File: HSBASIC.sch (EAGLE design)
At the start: 25 parts, among them IC1 ESP12SMT, IC3 MS563702BA03, IC4 DHT12

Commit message: Routing
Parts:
- removed R3: 10K, freetronics-jon:RESISTOR0603
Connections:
- removed net N$11: LED3.A, R7.1
- new net N$5: LED2.C, R10.2
- net 3.3V: now also LED2.A, LED3.A; no longer R3.2
- net GND: no longer LED2.C, LED3.C
- net GPIO16: no longer R10.2, R7.2
- net GPIO2: now also R10.1, R7.1; no longer R3.1
- net N$4: now also LED3.C, R7.2; no longer LED2.A, R10.1
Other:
- note added: "Change sensor to BME280. 20 bought in Jan 2018. Find them! Barometric Pressure Sensor: MS5637-02BA03 Pressure range: 1kpa to 200kpa (0.145psi to 29psi) Temperature range: -40C to +85C Temperature resolution: 0.01C Temperature accuracy: +/- 1C I2C address: 0xED Humidity / Temperature Sensor: DHT12 Humidity range: 20 to 95% Humidity resolution: 0.1% Humidity precision: +/- 5% Temperature range: -20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"
- note added: "GPIO0: Bias HIGH GPIO2: Bias HIGH GPIO15: Bias LOW CH_PD: Bias HIGH GPIO2: Status LED active low From D1 Mini profile for Arduino: GPIO4: D2 SDA GPIO5: D1 SCL From Sonoff: GPIO2: SDA GPIO14: SCL From Tasmota: GPIO4: SDA GPIO14: SCL"
- note removed: "Barometric Pressure Sensor: MS5637-02BA03 Pressure range: 1kpa to 200kpa (0.145psi to 29psi) Temperature range: -40C to +85C Temperature resolution: 0.01C Temperature accuracy: +/- 1C I2C address: 0xED Humidity / Temperature Sensor: DHT12 Humidity range: 20 to 95% Humidity resolution: 0.1% Humidity precision: +/- 5% Temperature range: -20 to +60C Temperature resolution: 0.1C Temperature precision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"
- note removed: "GPIO0: Bias HIGH GPIO2: Bias HIGH GPIO15: Bias LOW CH_PD: Bias HIGH GPIO16: Status LED From D1 Mini profile for Arduino: GPIO4: D2 SDA GPIO5: D1 SCL From Sonoff: GPIO2: SDA GPIO14: SCL From Tasmota: GPIO4: SDA GPIO14: SCL"
- moved on the sheet: LED2, LED3, R10, R7

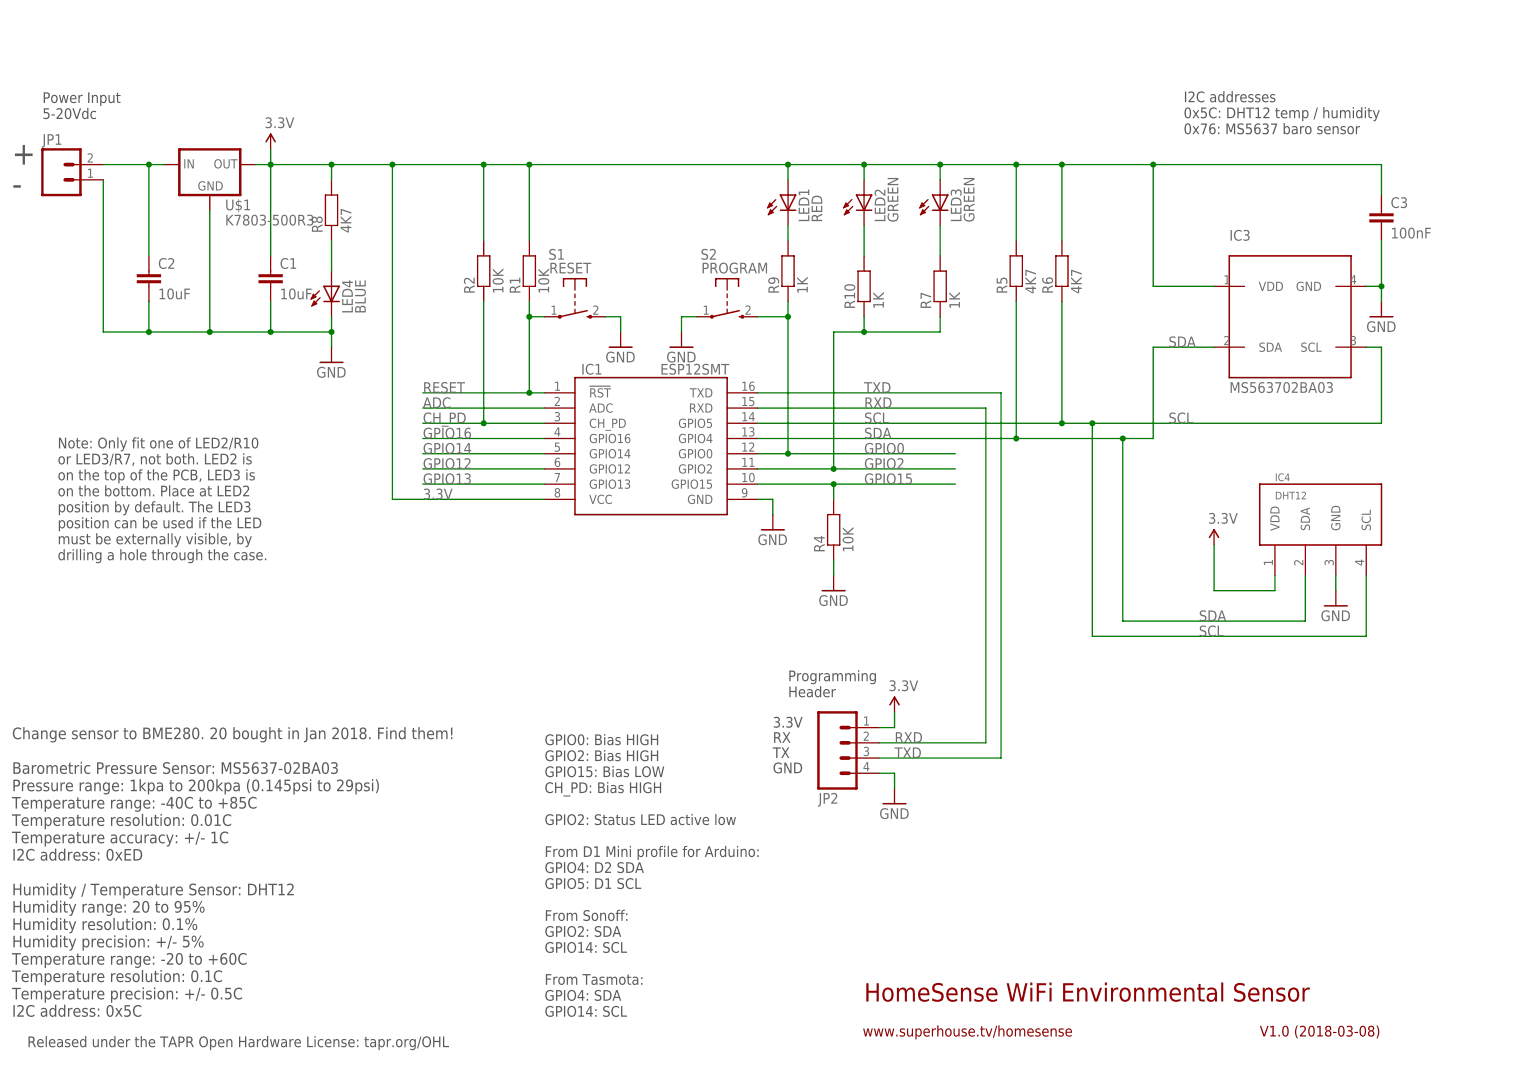
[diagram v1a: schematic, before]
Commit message: Switch to BME280 sensor for Tasmota compatibility
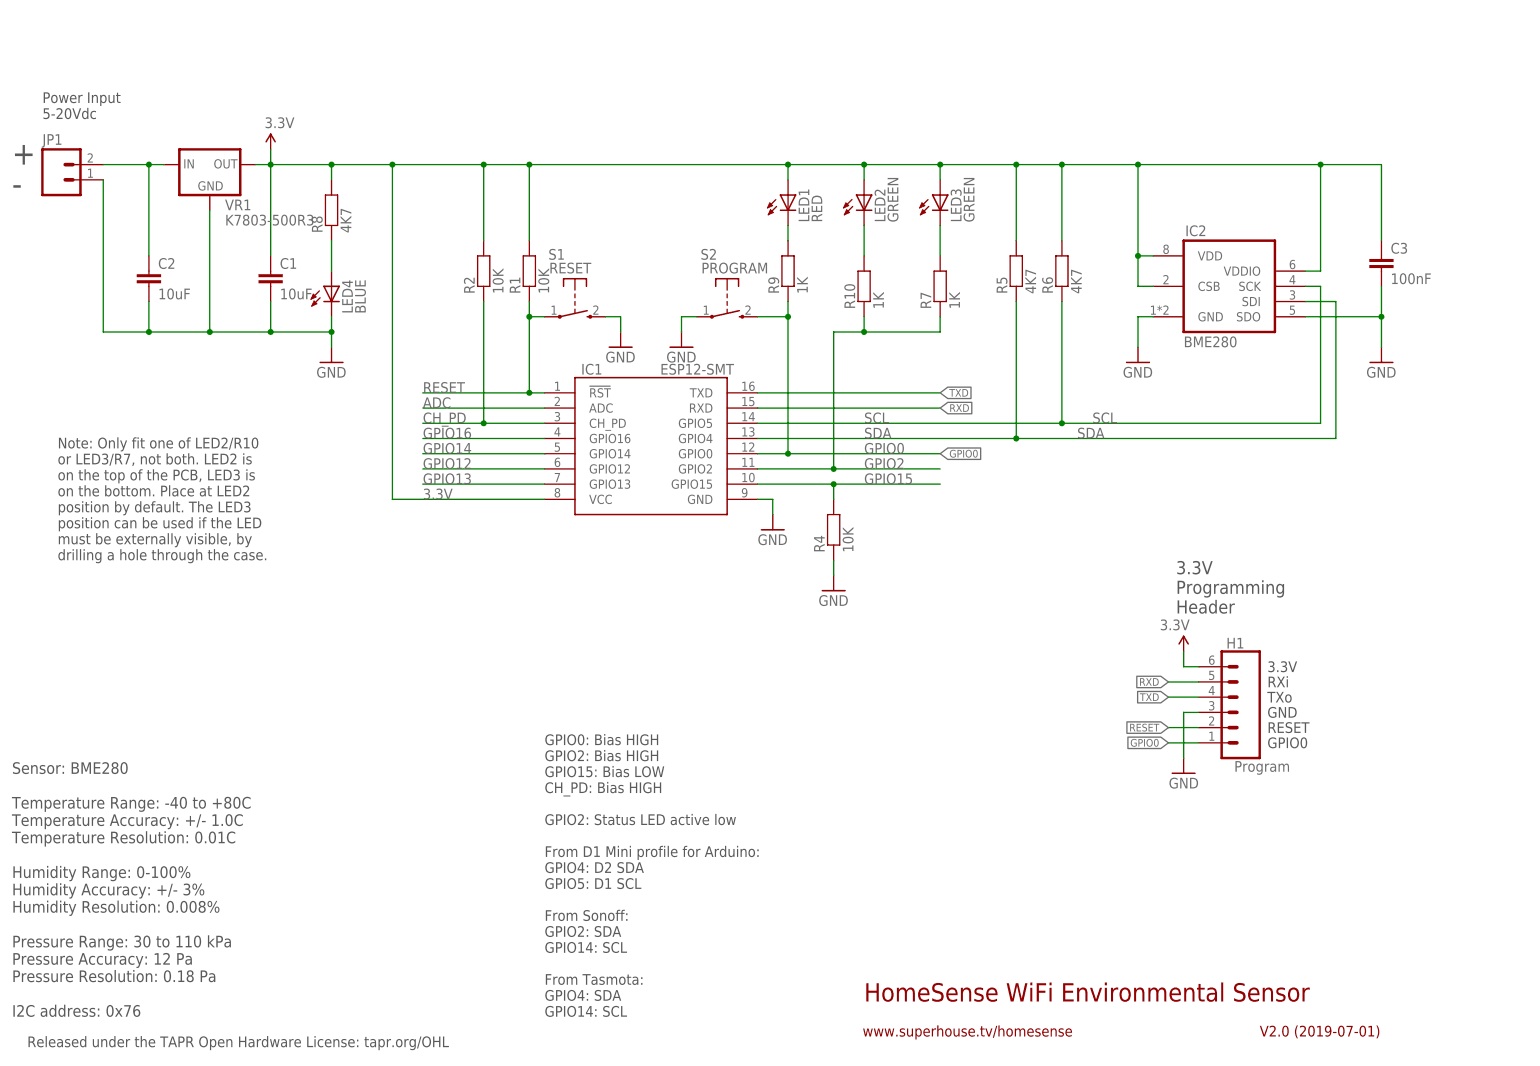
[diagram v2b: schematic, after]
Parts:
- removed IC3: MS563702BA03, freetronics-jon:MS563702BA03
- removed IC4: DHT12, freetronics-jon:DHT12FLAT
- removed JP2: (no value), freetronics-jon:M04PTH
- removed U$1: K7803-500R3, freetronics-jon:K78XX-500R3
- added H1: Program, SuperHouse-Connectors:M06-SOCKET
- added IC2: BME280, SuperHouse-Sensors:BME280
- added VR1: K7803-500R3, SuperHouse-Regulators:K78XX-500R3
- C1, C2: device freetronics-jon:CAP0805 -> SuperHouse-DiscreteSemi:CAP1206
- C3: device freetronics-jon:CAP0603 -> SuperHouse-DiscreteSemi:CAP0603
- IC1: value ESP12SMT -> ESP12-SMT; device freetronics-jon:ESP12SMT -> SuperHouse-MCUs:ESP12-SMT
- LED1, LED2, LED3, LED4: device freetronics-jon:LED0603 -> SuperHouse-LEDs:LED0603
- R1, R10, R2, R4, R5, R6, R7, R8, R9: device freetronics-jon:RESISTOR0603 -> SuperHouse-DiscreteSemi:RESISTOR0603
- S1, S2: device freetronics-jon:TAC_SWITCH_2PINSMT -> SuperHouse-Switches:TAC_SWITCH_2PINSMT
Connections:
- net 3.3V: now also H1.6, IC2.CSB, IC2.VDD, IC2.VDDIO, VR1.OUT; no longer IC3.VDD, IC4.VDD, JP2.1, U$1.OUT
- net GND: now also H1.3, IC2.GND, IC2.SDO, VR1.GND; no longer IC3.GND, IC4.GND, JP2.4, U$1.GND
- net GPIO0: now also H1.1
- net N$1: now also VR1.IN; no longer U$1.IN
- net RESET: now also H1.2
- net RXD: now also H1.5; no longer JP2.2
- net SCL: now also IC2.SCK; no longer IC3.SCL, IC4.SCL
- net SDA: now also IC2.SDI; no longer IC3.SDA, IC4.SDA
- net TXD: now also H1.4; no longer JP2.3
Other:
- note added: "3.3V Programming Header"
- note added: "GPIO0"
- note added: "RESET"
- note added: "RXi"
- note added: "Sensor: BME280 Temperature Range: -40 to +80C Temperature Accuracy: +/- 1.0C Temperature Resolution: 0.01C Humidity Range: 0-100% Humidity Accuracy: +/- 3% Humidity Resolution: 0.008% Pressure Range: 30 to 110 kPa Pressure Accuracy: 12 Pa Pressure Resolution: 0.18 Pa I2C address: 0x76"
- note added: "TXo"
- note added: "V2.0 (2019-07-01)"
- note removed: "Change sensor to BME280. 20 bought in Jan 2018. Find them! Barometric Pressure Sensor: MS5637-02BA03 Pressure range: 1kpa to 200kpa (0.145psi to 29psi) Temperature range: -40C to +85C Temperature resolution: 0.01C Temperature accuracy: +/- 1C I2C address: 0xED Humidity / Temperature Sensor: DHT12 Humidity range: 20 to 95% Humidity resolution: 0.1% Humidity precision: +/- 5% Temperature range: -20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"
- note removed: "I2C addresses 0x5C: DHT12 temp / humidity 0x76: MS5637 baro sensor"
- note removed: "Programming Header"
- note removed: "RX"
- note removed: "TX"
- note removed: "V1.0 (2018-03-08)"
- moved on the sheet: C3

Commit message: Routing progress
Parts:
- removed H1: Program, SuperHouse-Connectors:M06-SOCKET
- added J1: ESPROG-SOCKET, SuperHouse-Connectors:ESPROG-SOCKET
- added J2: (no value), SuperHouse-Connectors:M04-PLAIN
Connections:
- removed net RESET: H1.2, IC1.!RST, R1.1, S1.P
- new net !RESET: IC1.!RST, J1.6, R1.1, S1.P
- net 3.3V: now also J1.3, J2.3; no longer H1.6
- net GND: now also J1.1, J2.4; no longer H1.3
- net GPIO0: now also J1.2; no longer H1.1
- net RXD: now also J1.4; no longer H1.5
- net SCL: now also J2.2
- net SDA: now also J2.1
- net TXD: now also J1.5; no longer H1.4
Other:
- note added: "GPIO0: Bias HIGH GPIO2: Bias HIGH GPIO15: Bias LOW CH_PD: Bias HIGH GPIO2: Status LED active low GPIO4: SDA GPIO5: SCL"
- note removed: "3.3V"
- note removed: "GND"
- note removed: "GPIO0"
- note removed: "GPIO0: Bias HIGH GPIO2: Bias HIGH GPIO15: Bias LOW CH_PD: Bias HIGH GPIO2: Status LED active low From D1 Mini profile for Arduino: GPIO4: D2 SDA GPIO5: D1 SCL From Sonoff: GPIO2: SDA GPIO14: SCL From Tasmota: GPIO4: SDA GPIO14: SCL"
- note removed: "RESET"
- note removed: "RXi"
- note removed: "TXo"
- moved on the sheet: C1, C2, C3, IC1, IC2, JP1, LED1, LED2, LED3, LED4, R1, R10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

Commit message: Routing I2C
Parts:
- added FID1, FID2, FID3: FIDUCIAL1X2.5, freetronics:FIDUCIAL1X2.5
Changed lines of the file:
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@@
 <part name="GND4" library="SuperHouse-SupplySymbols" library_urn="urn:adsk.eagle:library:11790503" deviceset="GND" device=""/>
 <part name="P+3" library="SuperHouse-SupplySymbols" library_urn="urn:adsk.eagle:library:11790503" deviceset="3.3V" device=""/>
+<part name="FID1" library="freetronics" deviceset="FIDUCIAL" device="1X2.5"/>
+<part name="FID2" library="freetronics" deviceset="FIDUCIAL" device="1X2.5"/>
+<part name="FID3" library="freetronics" deviceset="FIDUCIAL" device="1X2.5"/>
 </parts>
 <sheets>
@@
 <attribute name="VALUE" x="72.644" y="64.516" size="1.778" layer="96"/>
 </instance>
+<instance part="FID1" gate="G$1" x="137.16" y="7.62" smashed="yes"/>
+<instance part="FID2" gate="G$1" x="142.24" y="7.62" smashed="yes"/>
+<instance part="FID3" gate="G$1" x="132.08" y="7.62" smashed="yes"/>
 </instances>
 <busses>

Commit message: Hopefully final routing for v2.0 release
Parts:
- removed FID1: FIDUCIAL1X2.5, freetronics:FIDUCIAL1X2.5
- C1, C2: device SuperHouse-DiscreteSemi:CAP1206 -> SuperHouse-DiscreteSemi:CAP0805
- J2: value (none) -> I2C
- JP1: value (none) -> PWR
- VR1: device SuperHouse-Regulators:K78XX-500R3 -> SuperHouse-Regulators:K78XX-500R3-FLAT
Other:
- note added: "ESProg Programming Header"
- note added: "HomeSense Basic WiFi Environmental Sensor"
- note added: "Prototyping Area"
- note added: "V2.0 (2019-09-09)"
- note added: "www.superhouse.tv/hsbasic"
- note removed: "3.3V Programming Header"
- note removed: "HomeSense WiFi Environmental Sensor"
- note removed: "V2.0 (2019-07-01)"
- note removed: "www.superhouse.tv/homesense"
- moved on the sheet: J2

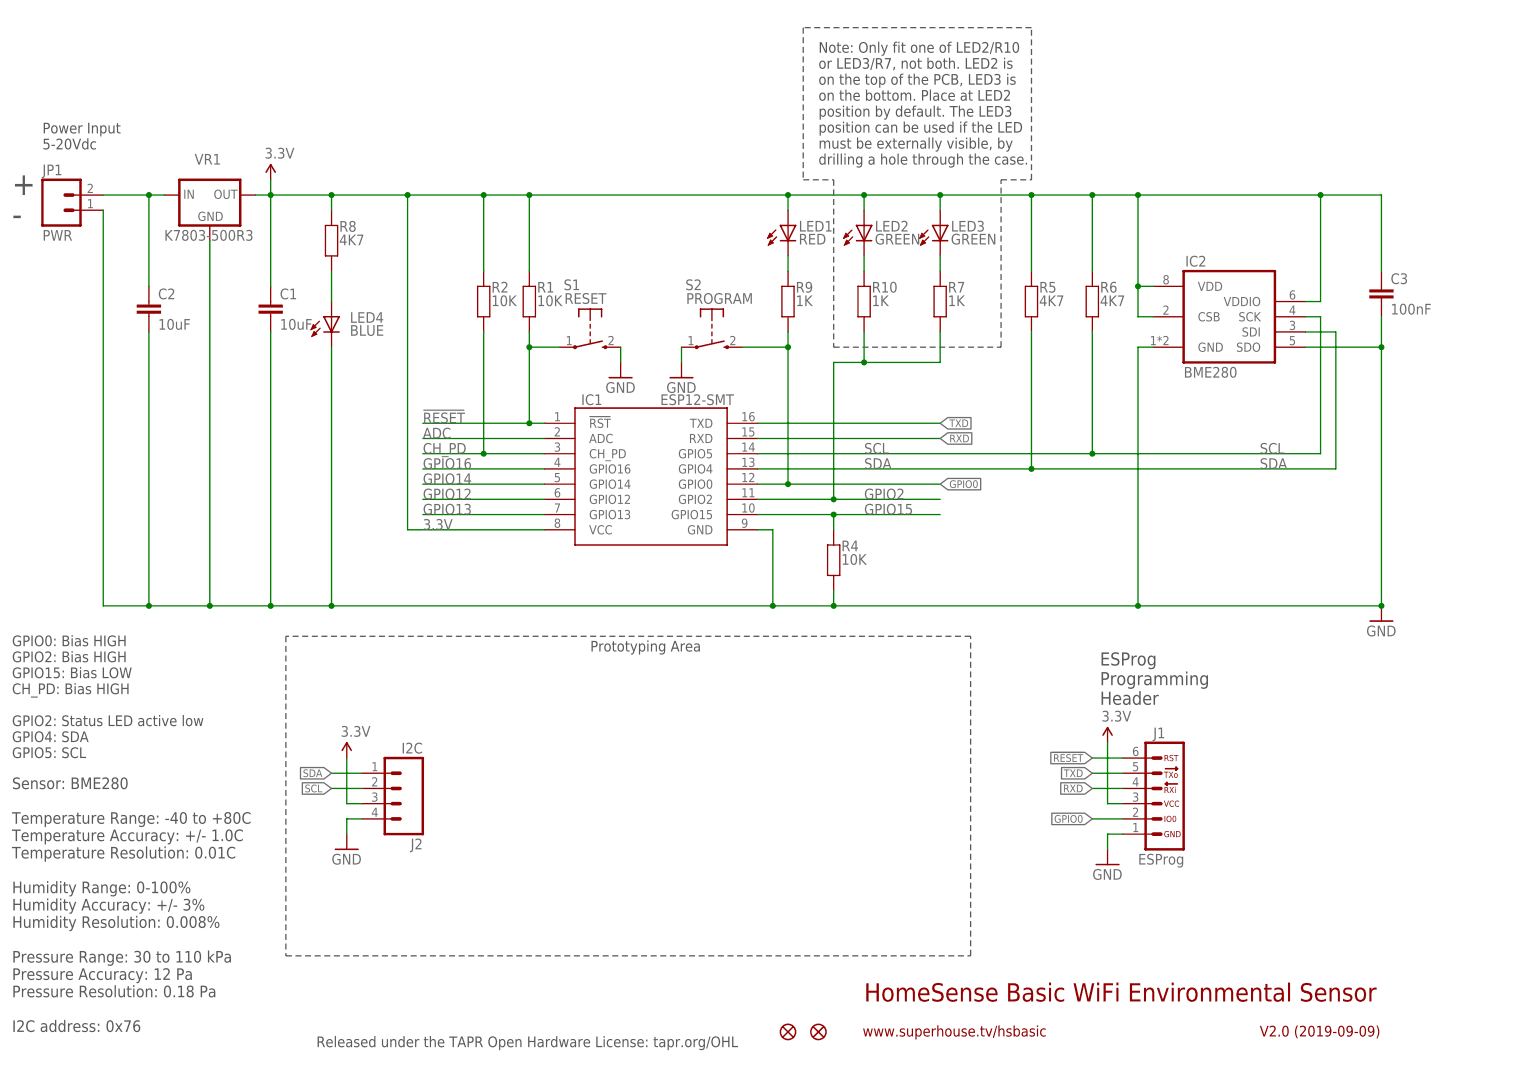
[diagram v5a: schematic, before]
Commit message: Major restructure to add OLED and prototyping area
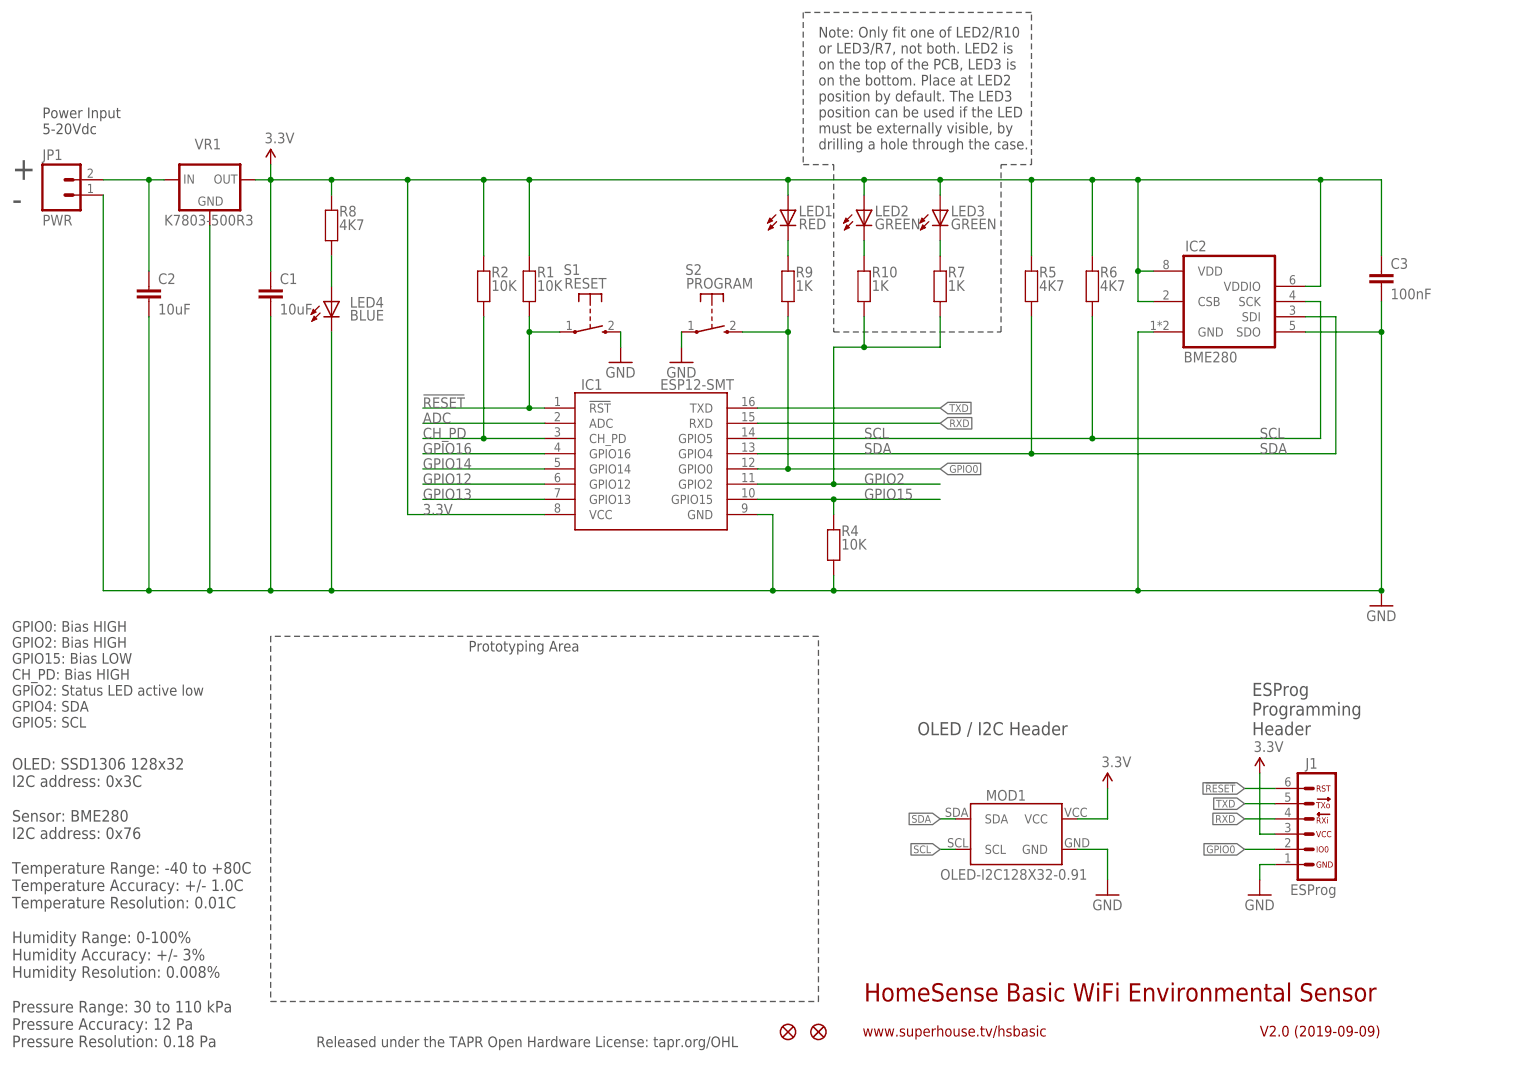
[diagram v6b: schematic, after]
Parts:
- removed J2: I2C, SuperHouse-Connectors:M04-PLAIN
- added MOD1: OLED-I2C128X32-0.91, SuperHouse-Displays:OLED-I2C128X32-0.91
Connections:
- net 3.3V: now also MOD1.VCC; no longer J2.3
- net GND: now also MOD1.GND; no longer J2.4
- net SCL: now also MOD1.SCL; no longer J2.2
- net SDA: now also MOD1.SDA; no longer J2.1
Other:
- note added: "OLED / I2C Header"
- note added: "OLED: SSD1306 128x32 I2C address: 0x3C Sensor: BME280 I2C address: 0x76 Temperature Range: -40 to +80C Temperature Accuracy: +/- 1.0C Temperature Resolution: 0.01C Humidity Range: 0-100% Humidity Accuracy: +/- 3% Humidity Resolution: 0.008% Pressure Range: 30 to 110 kPa Pressure Accuracy: 12 Pa Pressure Resolution: 0.18 Pa"
- note removed: "Sensor: BME280 Temperature Range: -40 to +80C Temperature Accuracy: +/- 1.0C Temperature Resolution: 0.01C Humidity Range: 0-100% Humidity Accuracy: +/- 3% Humidity Resolution: 0.008% Pressure Range: 30 to 110 kPa Pressure Accuracy: 12 Pa Pressure Resolution: 0.18 Pa I2C address: 0x76"
- moved on the sheet: C1, C2, C3, IC1, IC2, J1, JP1, LED1, LED2, LED3, LED4, R1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
